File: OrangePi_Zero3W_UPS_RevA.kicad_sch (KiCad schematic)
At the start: 21 parts, among them J1 ORANGE_PI_ZERO_3W_HEADER, J2 BATTERY_1S_PROTECTED_NTC, SW1 POWER / QON, U1 MAX17048G_T10, U2 BQ25895RTWR

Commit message: Update OrangePi_Zero3W_UPS_RevA.kicad_sch
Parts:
- added J3: USB_C_POWER_INPUT, Connector_USB:USB_C_Receptacle_JAE_DX07S016JA1R1500, symbol Connector:USB_C_Receptacle_USB2.0_16P
- added U3: STUSB4500LQTR, STUSB4500LQTR:QFN50P400X400X100-25N, symbol STUSB4500LQTR:STUSB4500LQTR
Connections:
- new net: J3.A1 (GND), J3.A12 (GND), J3.B1 (GND), J3.B12 (GND)
- new net: J3.A4 (VBUS), J3.A9 (VBUS), J3.B4 (VBUS), J3.B9 (VBUS)

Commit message: Phase 5B.2B: connect USB-C CC, data and STUSB4500L core
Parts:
- added C8, C9: 1uF, Capacitor_SMD:C_0603_1608Metric, symbol Device:C
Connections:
- net GND: now also J3.A1 (GND), J3.A12 (GND), J3.B1 (GND), J3.B12 (GND), J3.S1 (SHIELD), U3.10 (GND), U3.12 (ADDR0), U3.13 (ADDR1), U3.22 (VSYS), U3.25 (EXP), U3.3 (NU), U3.6 (RESET), C8.2, C9.2
- net I2C_SCL: now also U3.7 (SCL)
- net I2C_SDA: now also U3.8 (SDA)
- net USB_DP: now reaches U2.2 (D+)
- net USB_DP: now also J3.A6 (D+), J3.B6 (D+)
- net USB_DM: now reaches U2.3 (D–)
- net USB_DM: now also J3.A7 (D-), J3.B7 (D-)
- net USB_CC1: now reaches U3.1 (CC1DB)
- net USB_CC1: now also J3.A5 (CC1), U3.2 (CC1)
- net at U3.21 (VREG_1V2): now also C8.1
- net at U3.23 (VREG_2V7): now also C9.1
- net USB_VBUS_RAW: now reaches U3.24 (VDD)
- net USB_VBUS_RAW: now also J3.A4 (VBUS), J3.A9 (VBUS), J3.B4 (VBUS), J3.B9 (VBUS)
- net USB_CC2: now reaches U3.4 (CC2)
- net USB_CC2: now also J3.B5 (CC2), U3.5 (CC2DB)
- no-connect marks 30 -> 38
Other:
- note added: "STUSB4500L I2C address: 0x28 ADDR1=0, ADDR0=0"
- moved on the sheet: J3, U3

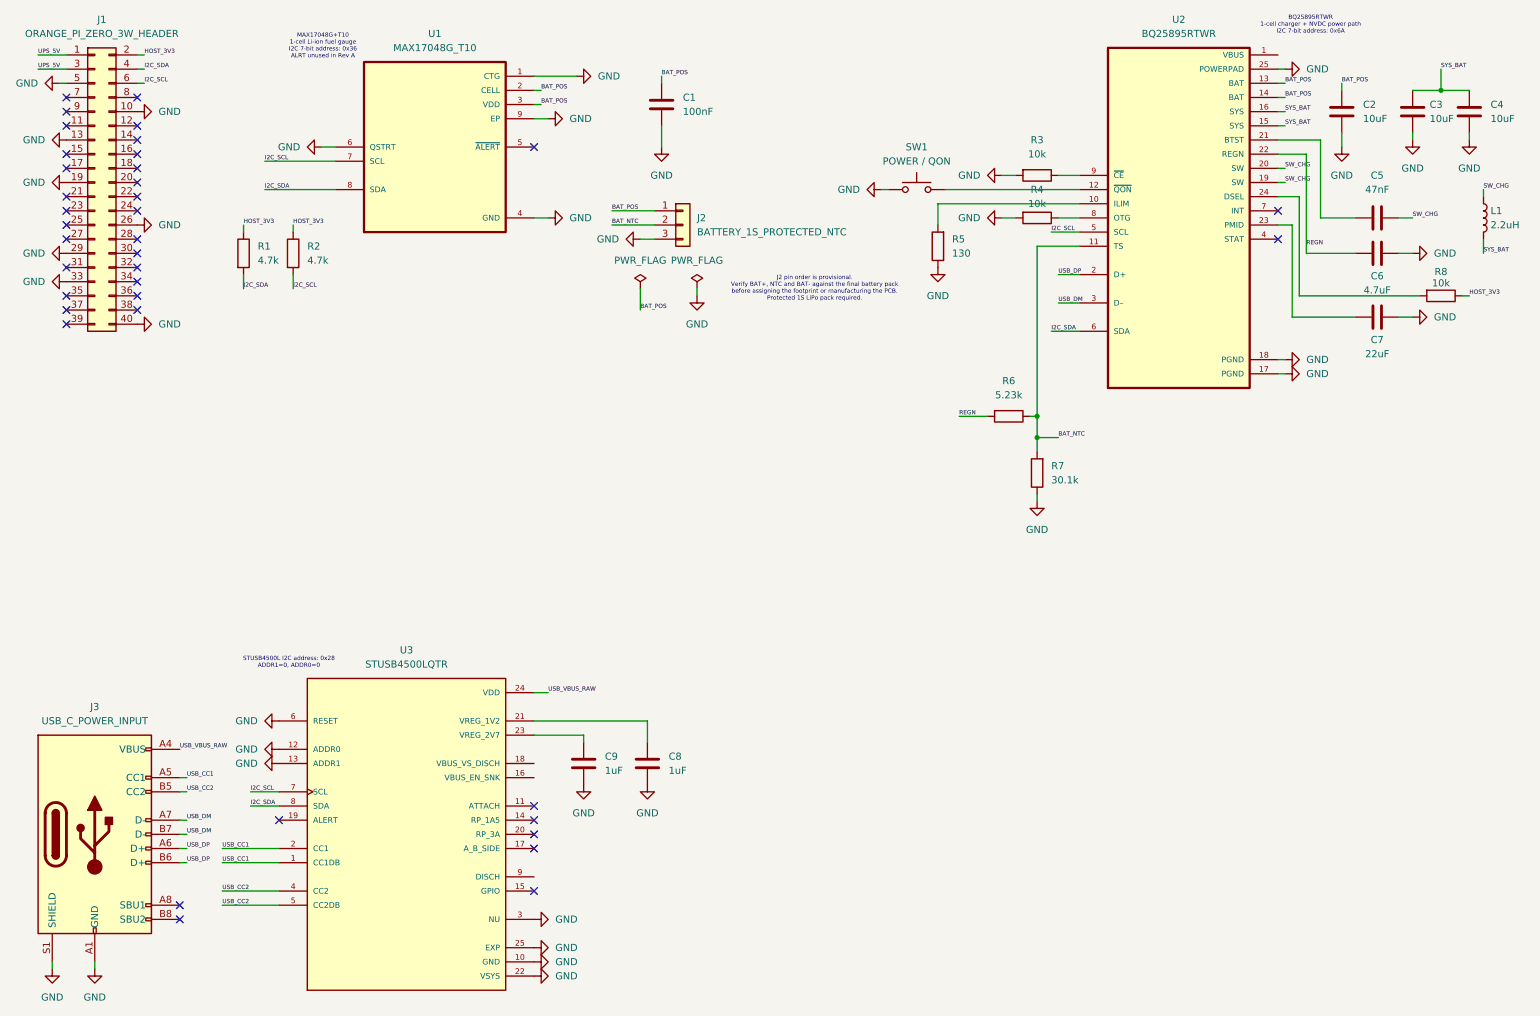
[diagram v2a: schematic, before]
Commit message: Phase 5B.2C: add USB-C VBUS switch and monitoring path
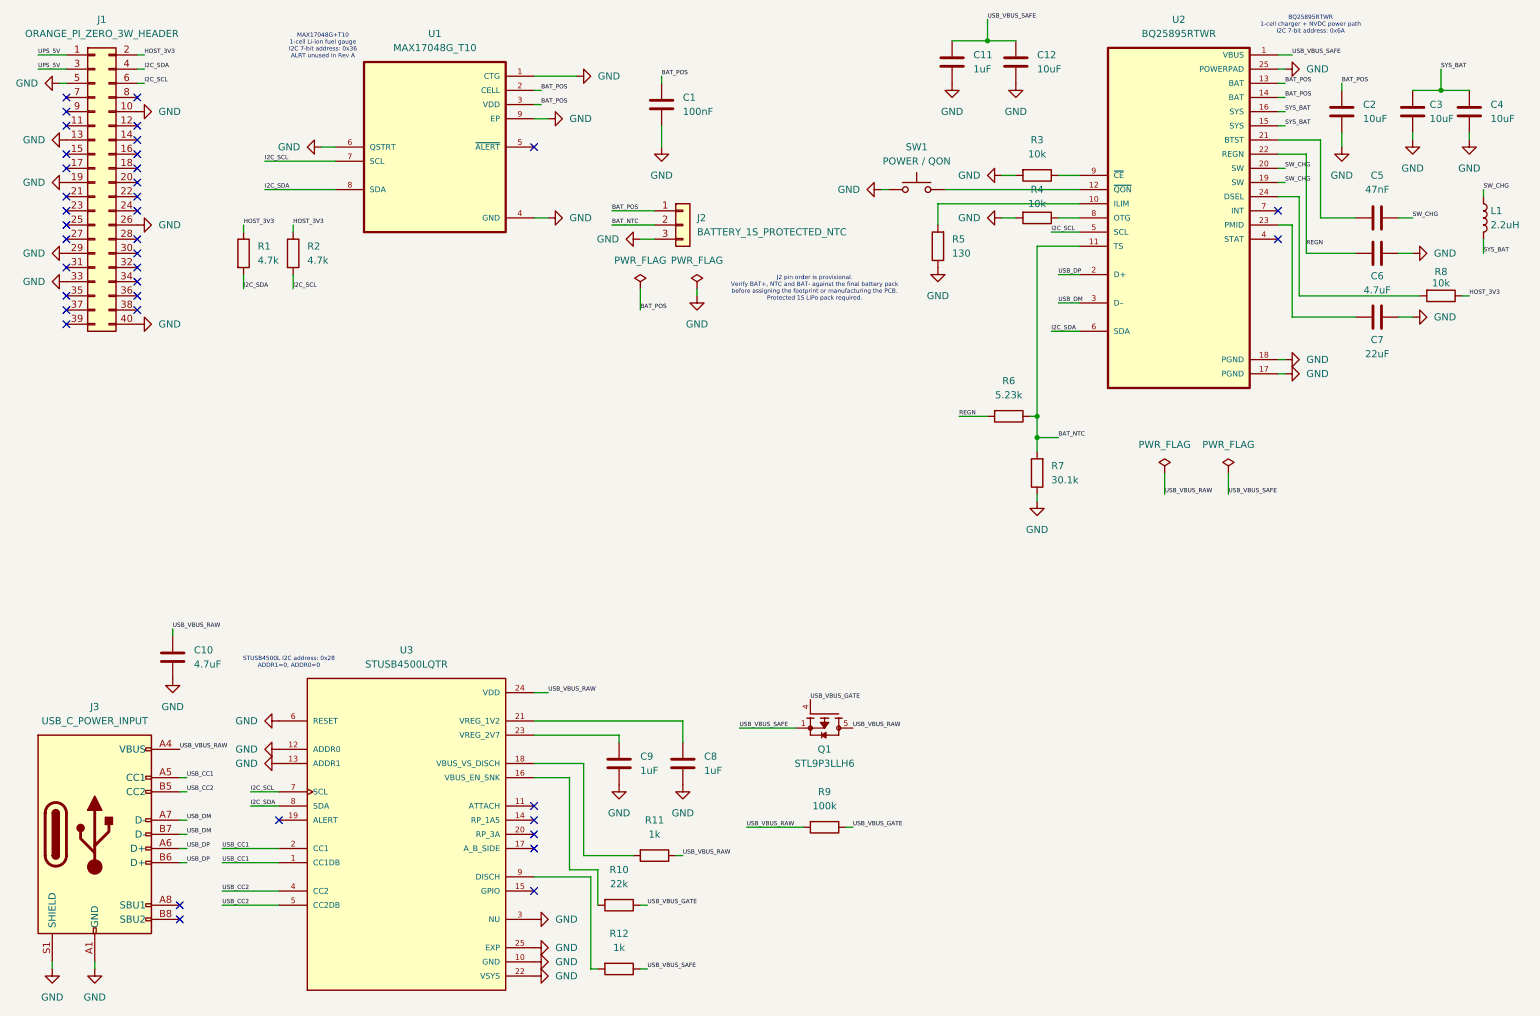
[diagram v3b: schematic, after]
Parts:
- added C10: 4.7uF, Capacitor_SMD:C_0805_2012Metric, symbol Device:C
- added C11: 1uF, Capacitor_SMD:C_0805_2012Metric, symbol Device:C
- added C12: 10uF, Capacitor_SMD:C_0805_2012Metric, symbol Device:C
- added Q1: STL9P3LLH6, STL9P3LLH6:TRANS_STL9P3LLH6, symbol STL9P3LLH6:STL9P3LLH6
- added R10: 22k, Resistor_SMD:R_0603_1608Metric, symbol Device:R
- added R11, R12: 1k, Resistor_SMD:R_0603_1608Metric, symbol Device:R
- added R9: 100k, Resistor_SMD:R_0603_1608Metric, symbol Device:R
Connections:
- net GND: now also C10.2, C11.2, C12.2
- net USB_VBUS_RAW: now also C10.1, Q1.5, Q1.5_1, Q1.5_2, R11.1, R9.2
- net USB_VBUS_SAFE: now reaches U2.1 (VBUS)
- net USB_VBUS_SAFE: now also C11.1, C12.1, Q1.1, Q1.2, Q1.3, R12.1
- net at U3.16 (VBUS_EN_SNK): now also R10.2
- net at U3.18 (VBUS_VS_DISCH): now also R11.2
- net at U3.9 (DISCH): now also R12.2
- new net USB_VBUS_GATE: Q1.4, R10.1, R9.1
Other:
- moved on the sheet: C8, C9
